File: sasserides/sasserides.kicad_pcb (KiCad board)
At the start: 2 copper layers, 170 x 80 mm, 128 parts, among them J1 Conn_02x16_Odd_Even, Q1 2N7002

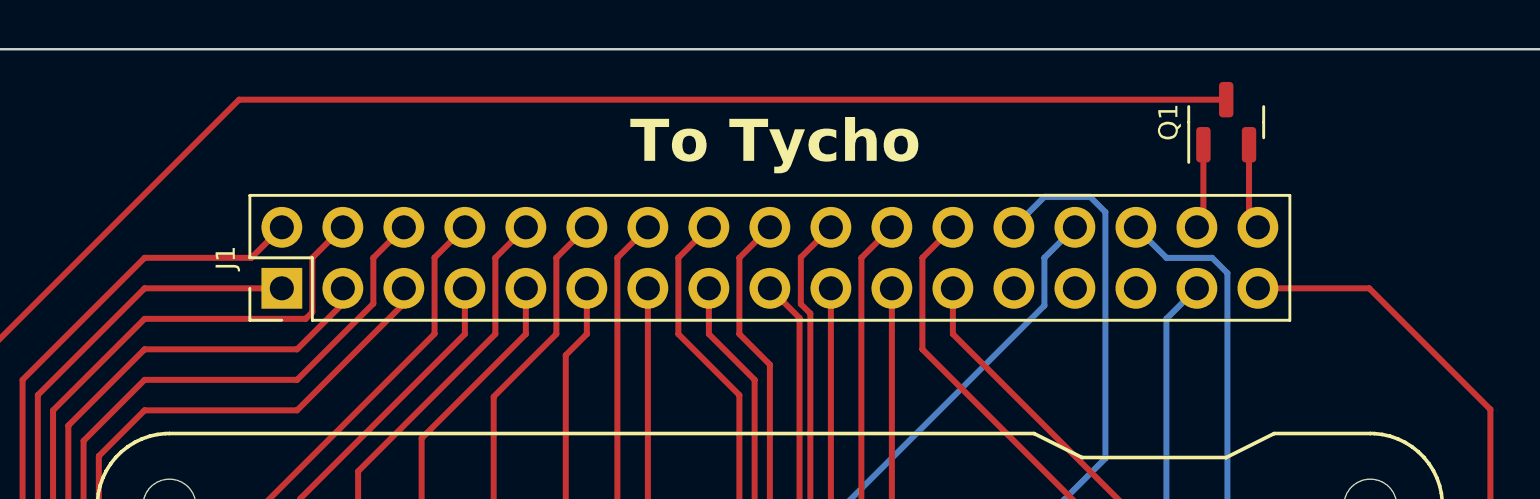
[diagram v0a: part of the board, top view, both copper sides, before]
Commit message: Change 34 pin header on Sasserides-A to shrouded type.
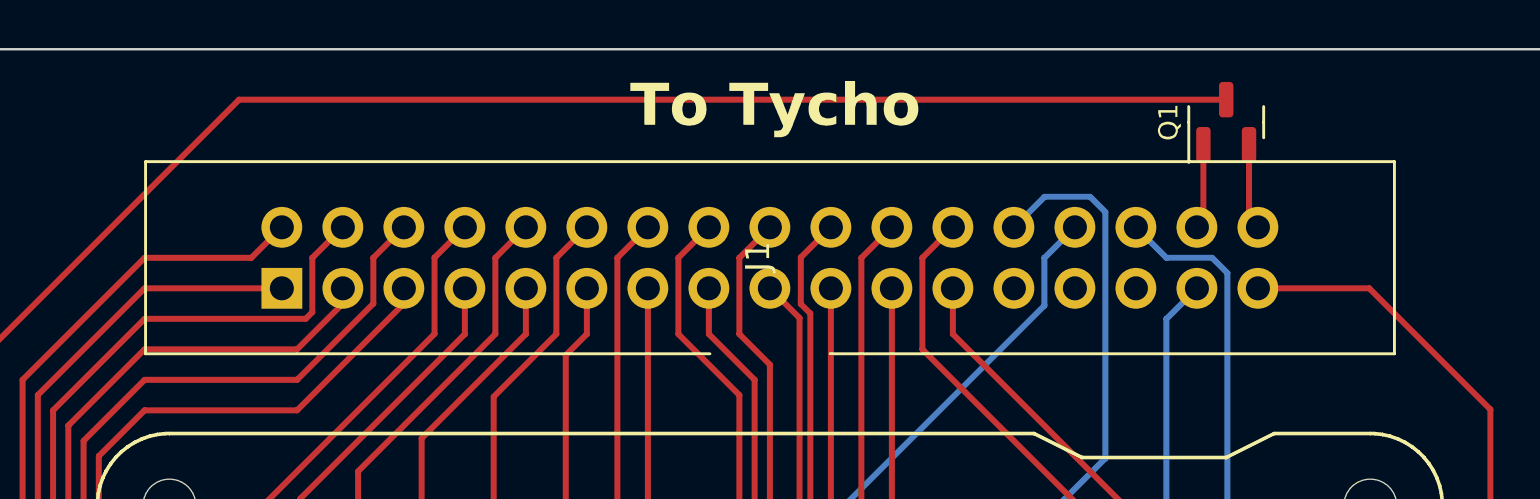
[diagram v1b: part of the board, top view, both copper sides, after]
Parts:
- J1: footprint Connector_PinHeader_2.54mm:PinHeader_2x17_P2.54mm_Vertical -> tycho:shrouded_pin-header_2x17
- moved J1 20.4 mm to (100.0, 68.7)

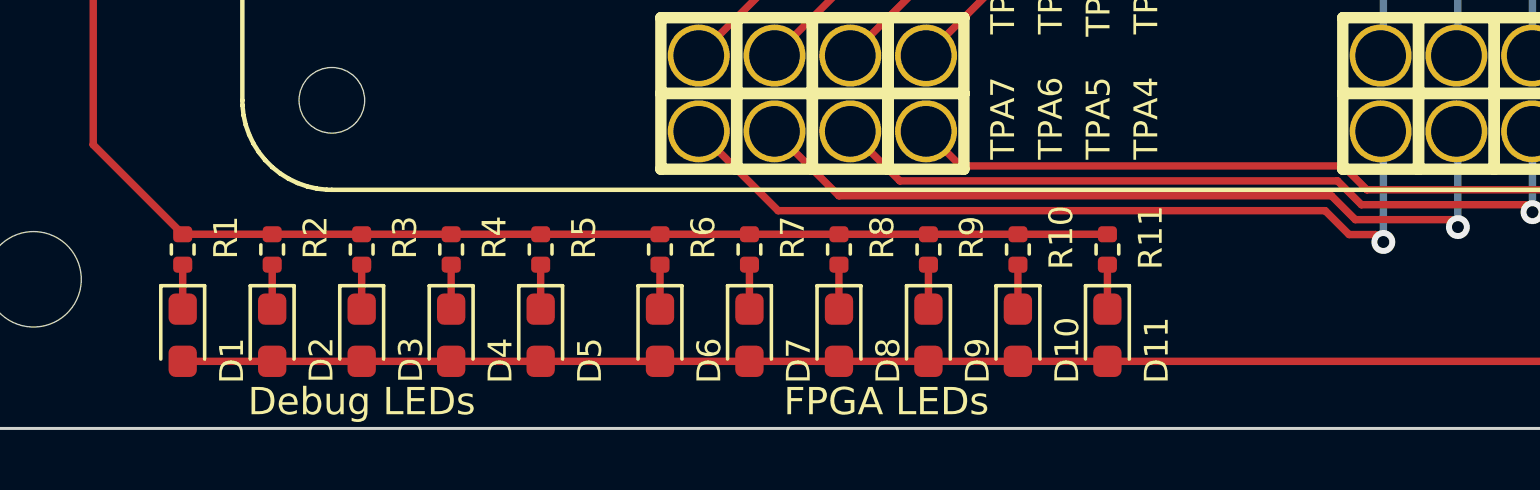
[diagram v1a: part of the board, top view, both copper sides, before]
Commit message: Increase spacing between Sasserides-A LED groups.
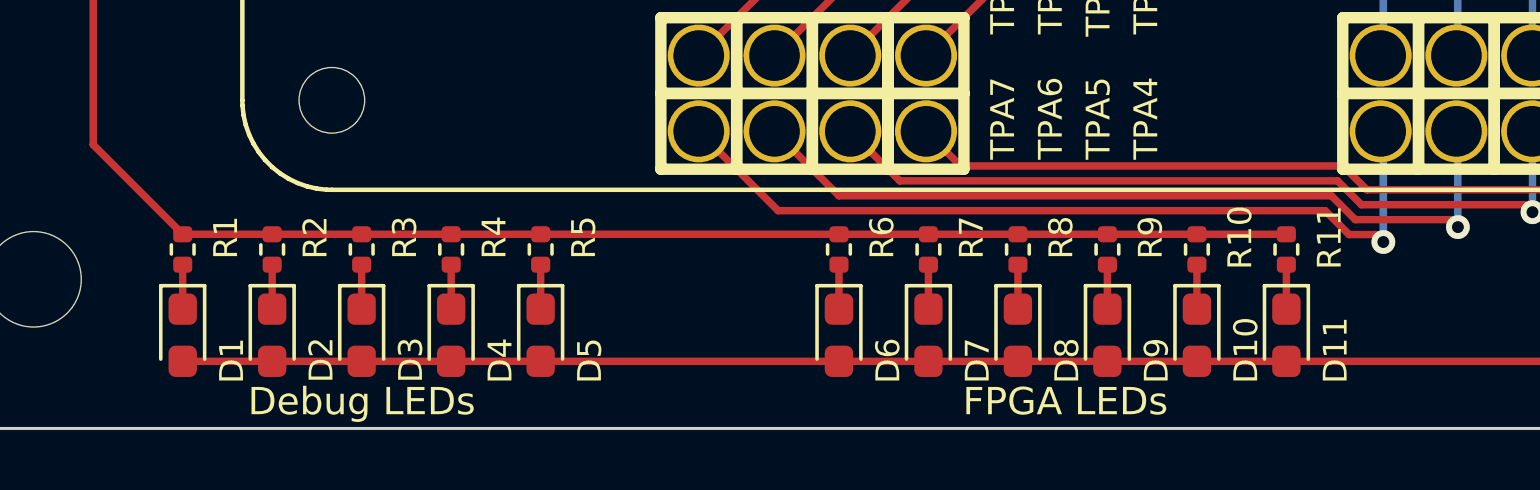
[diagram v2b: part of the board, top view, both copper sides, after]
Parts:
- moved D10 6.00 mm to (104.0, 136.9)
- moved D11 6.00 mm to (107.0, 136.9)
- moved D6 6.00 mm to (92.0, 136.9)
- moved D7 6.00 mm to (95.0, 136.9)
- moved D8 6.00 mm to (98.0, 136.9)
- moved D9 6.00 mm to (101.0, 136.9)
- moved R10 6.00 mm to (104.0, 134.0)
- moved R11 6.00 mm to (107.0, 134.0)
- moved R6 6.00 mm to (92.0, 134.0)
- moved R7 6.00 mm to (95.0, 134.0)
- moved R8 6.00 mm to (98.0, 134.0)
- moved R9 6.00 mm to (101.0, 134.0)
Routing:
- net Net-(Q1-D): track 149.2 -> 155.2 mm
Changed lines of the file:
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@@
   )
   (footprint "LED_SMD:LED_0603_1608Metric_Pad1.05x0.95mm_HandSolder" (layer "F.Cu")
-    (at 92 136.875 -90)
+    (at 98 136.875 -90)
     (descr "LED SMD 0603 (1608 Metric), square (rectangular) end terminal, IPC_7351 nominal, (Body size source: http://www.tortai-tech.com/upload/download/2011102023233369053.pdf), generated with kicad-footprint-generator")
     (tags "LED handsolder")
@@
   )
   (footprint "LED_SMD:LED_0603_1608Metric_Pad1.05x0.95mm_HandSolder" (layer "F.Cu")
-    (at 101 136.875 -90)
+    (at 107 136.875 -90)
     (descr "LED SMD 0603 (1608 Metric), square (rectangular) end terminal, IPC_7351 nominal, (Body size source: http://www.tortai-tech.com/upload/download/2011102023233369053.pdf), generated with kicad-footprint-generator")
     (tags "LED handsolder")
@@
   )
   (footprint "LED_SMD:LED_0603_1608Metric_Pad1.05x0.95mm_HandSolder" (layer "F.Cu")
-    (at 95 136.875 -90)
+    (at 101 136.875 -90)
     (descr "LED SMD 0603 (1608 Metric), square (rectangular) end terminal, IPC_7351 nominal, (Body size source: http://www.tortai-tech.com/upload/download/2011102023233369053.pdf), generated with kicad-footprint-generator")
     (tags "LED handsolder")
@@
   )
   (footprint "Resistor_SMD:R_0402_1005Metric" (layer "F.Cu")
-    (at 86 134 90)
+    (at 92 134 90)
     (descr "Resistor SMD 0402 (1005 Metric), square (rectangular) end terminal, IPC_7351 nominal, (Body size source: IPC-SM-782 page 72, https://www.pcb-3d.com/wordpress/wp-content/uploads/ipc-sm-782a_amendment_1_and_2.pdf), generated with kicad-footprint-generator")
     (tags "resistor")
@@
   )
   (footprint "Resistor_SMD:R_0402_1005Metric" (layer "F.Cu")
-    (at 98 134 90)
+    (at 104 134 90)
     (descr "Resistor SMD 0402 (1005 Metric), square (rectangular) end terminal, IPC_7351 nominal, (Body size source: IPC-SM-782 page 72, https://www.pcb-3d.com/wordpress/wp-content/uploads/ipc-sm-782a_amendment_1_and_2.pdf), generated with kicad-footprint-generator")
     (tags "resistor")
@@
   )
   (footprint "LED_SMD:LED_0603_1608Metric_Pad1.05x0.95mm_HandSolder" (layer "F.Cu")
-    (at 98 136.875 -90)
+    (at 104 136.875 -90)
     (descr "LED SMD 0603 (1608 Metric), square (rectangular) end terminal, IPC_7351 nominal, (Body size source: http://www.tortai-tech.com/upload/download/2011102023233369053.pdf), generated with kicad-footprint-generator")
     (tags "LED handsolder")
@@
   )
   (footprint "Resistor_SMD:R_0402_1005Metric" (layer "F.Cu")
-    (at 89 134 90)
+    (at 95 134 90)
     (descr "Resistor SMD 0402 (1005 Metric), square (rectangular) end terminal, IPC_7351 nominal, (Body size source: IPC-SM-782 page 72, https://www.pcb-3d.com/wordpress/wp-content/uploads/ipc-sm-782a_amendment_1_and_2.pdf), generated with kicad-footprint-generator")
     (tags "resistor")
@@
   )
   (footprint "LED_SMD:LED_0603_1608Metric_Pad1.05x0.95mm_HandSolder" (layer "F.Cu")
-    (at 86 136.875 -90)
+    (at 92 136.875 -90)
     (descr "LED SMD 0603 (1608 Metric), square (rectangular) end terminal, IPC_7351 nominal, (Body size source: http://www.tortai-tech.com/upload/download/2011102023233369053.pdf), generated with kicad-footprint-generator")
     (tags "LED handsolder")
@@
   )
   (footprint "LED_SMD:LED_0603_1608Metric_Pad1.05x0.95mm_HandSolder" (layer "F.Cu")
-    (at 89 136.875 -90)
+    (at 95 136.875 -90)
     (descr "LED SMD 0603 (1608 Metric), square (rectangular) end terminal, IPC_7351 nominal, (Body size source: http://www.tortai-tech.com/upload/download/2011102023233369053.pdf), generated with kicad-footprint-generator")
     (tags "LED handsolder")
@@
   )
   (footprint "Resistor_SMD:R_0402_1005Metric" (layer "F.Cu")
-    (at 95 134 90)
+    (at 101 134 90)
     (descr "Resistor SMD 0402 (1005 Metric), square (rectangular) end terminal, IPC_7351 nominal, (Body size source: IPC-SM-782 page 72, https://www.pcb-3d.com/wordpress/wp-content/uploads/ipc-sm-782a_amendment_1_and_2.pdf), generated with kicad-footprint-generator")
     (tags "resistor")
@@
   )
   (footprint "Resistor_SMD:R_0402_1005Metric" (layer "F.Cu")
-    (at 92 134 90)
+    (at 98 134 90)
     (descr "Resistor SMD 0402 (1005 Metric), square (rectangular) end terminal, IPC_7351 nominal, (Body size source: IPC-SM-782 page 72, https://www.pcb-3d.com/wordpress/wp-content/uploads/ipc-sm-782a_amendment_1_and_2.pdf), generated with kicad-footprint-generator")
     (tags "resistor")
@@
   )
   (footprint "Resistor_SMD:R_0402_1005Metric" (layer "F.Cu")
-    (at 101 134 90)
+    (at 107 134 90)
     (descr "Resistor SMD 0402 (1005 Metric), square (rectangular) end terminal, IPC_7351 nominal, (Body size source: IPC-SM-782 page 72, https://www.pcb-3d.com/wordpress/wp-content/uploads/ipc-sm-782a_amendment_1_and_2.pdf), generated with kicad-footprint-generator")
     (tags "resistor")
@@
     (effects (font (size 1.75 1.75) (thickness 0.3) bold) (justify left bottom))
   )
-  (gr_text "FPGA LEDs" (at 93.59 139.1) (layer "F.SilkS")
+  (gr_text "FPGA LEDs" (at 99.59 139.1) (layer "F.SilkS")
     (effects (font (size 0.9144 0.9238) (thickness 0.15)))
   )
@@
   (segment (start 79 136) (end 79 134.51) (width 0.25) (layer "F.Cu") (net 5))
   (segment (start 82 136) (end 82 134.51) (width 0.25) (layer "F.Cu") (net 6))
-  (segment (start 86 136) (end 86 134.51) (width 0.25) (layer "F.Cu") (net 7))
-  (segment (start 89 136) (end 89 134.51) (width 0.25) (layer "F.Cu") (net 8))
-  (segment (start 92 136) (end 92 134.51) (width 0.25) (layer "F.Cu") (net 9))
-  (segment (start 95 136) (end 95 134.51) (width 0.25) (layer "F.Cu") (net 10))
-  (segment (start 98 136) (end 98 134.51) (width 0.25) (layer "F.Cu") (net 11))
-  (segment (start 101 136) (end 101 134.51) (width 0.25) (layer "F.Cu") (net 12))
+  (segment (start 92 136) (end 92 134.51) (width 0.25) (layer "F.Cu") (net 7))
+  (segment (start 95 136) (end 95 134.51) (width 0.25) (layer "F.Cu") (net 8))
+  (segment (start 98 136) (end 98 134.51) (width 0.25) (layer "F.Cu") (net 9))
+  (segment (start 101 136) (end 101 134.51) (width 0.25) (layer "F.Cu") (net 10))
+  (segment (start 104 136) (end 104 134.51) (width 0.25) (layer "F.Cu") (net 11))
+  (segment (start 107 136) (end 107 134.51) (width 0.25) (layer "F.Cu") (net 12))
   (segment (start 82.1 122.2) (end 79.22 122.2) (width 0.25) (layer "F.Cu") (net 13))
   (segment (start 69.52 74.4) (end 73.965 69.955) (width 0.25) (layer "F.Cu") (net 13))
@@
   (segment (start 119.95 67.045) (end 120.32 67.415) (width 0.25) (layer "F.Cu") (net 45))
   (segment (start 119.95 63.975) (end 119.95 67.045) (width 0.25) (layer "F.Cu") (net 45))
-  (segment (start 101 133.49) (end 70 133.49) (width 0.25) (layer "F.Cu") (net 46))
   (segment (start 67 130.49) (end 70 133.49) (width 0.25) (layer "F.Cu") (net 46))
   (segment (start 67 73) (end 67 130.49) (width 0.25) (layer "F.Cu") (net 46))
   (segment (start 77.9 62.1) (end 67 73) (width 0.25) (layer "F.Cu") (net 46))
+  (segment (start 107 133.49) (end 70 133.49) (width 0.25) (layer "F.Cu") (net 46))
   (segment (start 119 62.1) (end 77.9 62.1) (width 0.25) (layer "F.Cu") (net 46))
   (segment (start 96.92 125.5) (end 117.75 125.5) (width 0.25) (layer "F.Cu") (net 47))
